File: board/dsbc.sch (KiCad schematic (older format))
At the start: 3 parts

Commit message: dev
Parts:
- removed U?: XC9572XL-VQ44, symbol custom:XC9572XL-VQ44
- added C?: 100n, symbol Device:C_Small
- added R?: R_Small, symbol Device:R_Small
- added U?: XC95144XL-TQ100, Package_QFP:TQFP-100_14x14mm_P0.5mm, symbol CPLD_Xilinx:XC95144XL-TQ100
- added U?: IS61C5128AL-10TLI, Package_SO:TSOP-II-44_10.16x18.41mm_P0.8mm, symbol Memory_RAM:IS61C5128AL-10TLI
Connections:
- net labels added: +3V3, A1, A10, A11, A12, A13, A14, A15, A16, A17, A18, A19, A2, A20, A21, A22, A23, A3, A4, A5, A6, A7, A8, A9, ADDR_INC, BE, BOOT, CLK_40MHz, CLK_CPU, D0, D1, D2, D3, D4, D5, D6, D7, E, GND, MLB, MX, RDY, R~W, TCK, TDI, TDO, TMS, VALID_ADDR, VDA, VPA, VPB, ~ABORT, ~IRQ, ~NMI, ~RESET_CPU
- wire segments 0 -> 9
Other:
- note added: "VALID_ADDR = VPA & VDA"

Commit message: dev
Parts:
- removed U?: P8X32A, symbol custom:P8X32A
- removed U?: XC95144XL-TQ100, Package_QFP:TQFP-100_14x14mm_P0.5mm, symbol CPLD_Xilinx:XC95144XL-TQ100
- added C?: 100n, symbol Device:C_Small
- added J?: Prop Plug, symbol Connector:Conn_01x04_Male
- added R?: R_Small, symbol Device:R_Small
- added U?: P8X32A-D40, Package_DIP:DIP-40_W15.24mm, symbol MCU_Parallax:P8X32A-D40
- added U?: XC9572XL-VQ64, Package_QFP:TQFP-64_10x10mm_P0.5mm, symbol CPLD_Xilinx:XC9572XL-VQ64
- added U?: 24LC512, symbol Memory_EEPROM:24LC512
- added U?: PS2_female, symbol custom:PS2_female
- added Y?: Crystal, symbol Device:Crystal
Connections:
- net labels added: B, DB0, DB1, DB2, DB3, DB4, DB5, DB6, DB7, G, HSYNC, MEM_ACC, MISO, MOSI, PROP_RST, PS2_CLK, PS2_DATA, R, RX, SCL, SCLK, SDA, TX, VSYNC, ~CS0, ~CS1, ~PROP_RST, ~RAM_CE, ~RAM_OE, ~RAM_WE
- net labels removed: ADDR_INC
- wire segments 9 -> 39
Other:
- note added: "MEM_ACC = VALID_ADDR & CLK_CPU"
- moved on the sheet: R?

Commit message: add 16mbit sram symbol
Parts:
- removed U?: XC9572XL-VQ64, Package_QFP:TQFP-64_10x10mm_P0.5mm, symbol CPLD_Xilinx:XC9572XL-VQ64
- removed U?: IS61C5128AL-10TLI, Package_SO:TSOP-II-44_10.16x18.41mm_P0.8mm, symbol Memory_RAM:IS61C5128AL-10TLI
- added U2: IS61WV20488FBLL-10TLI, Package_SO:TSOP-II-44_10.16x18.41mm_P0.8mm, symbol custom:IS61WV20488FBLL-10TLI
- added U3: XC95144XL-TQ100, Package_QFP:TQFP-100_14x14mm_P0.5mm, symbol CPLD_Xilinx:XC95144XL-TQ100
- gave numbers to parts that had none: 10
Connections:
- net labels added: B0, B1, CLK_50MHz, G0, G1, G2, R0, R1, R2, STOP_CPU, ~CS2
- net labels removed: B, CLK_40MHz, G, R

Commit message: added ps/2 connector
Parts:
- removed U4: PS2_female, symbol custom:PS2_female
- added C10, C11, C12, C3, C4, C5, C6, C7, C8, C9: 100n, Capacitor_SMD:C_0805_2012Metric_Pad1.15x1.40mm_HandSolder, symbol Device:C_Small
- added J2: Mini-DIN-6, custom:MINI-DIN-6-FULL-SHIELD, symbol Connector:Mini-DIN-6
- added R3, R4: R_Small, Resistor_SMD:R_0805_2012Metric_Pad1.15x1.40mm_HandSolder, symbol Device:R_Small
- added R5: 10k, Resistor_SMD:R_0805_2012Metric_Pad1.15x1.40mm_HandSolder, symbol Device:R_Small
- added R6, R7: 2k2, Resistor_SMD:R_0805_2012Metric_Pad1.15x1.40mm_HandSolder, symbol Device:R_Small
- C1, C2: footprint (none) -> Capacitor_SMD:C_0805_2012Metric_Pad1.15x1.40mm_HandSolder
- J1: footprint (none) -> Connector_PinHeader_2.54mm:PinHeader_1x04_P2.54mm_Vertical
- R1, R2: footprint (none) -> Resistor_SMD:R_0805_2012Metric_Pad1.15x1.40mm_HandSolder
- U1: footprint (none) -> Package_DIP:DIP-40_W15.24mm
- U6: footprint (none) -> Package_DIP:DIP-8_W7.62mm_Socket
- Y1: footprint (none) -> Crystal:Resonator-2Pin_W10.0mm_H5.0mm
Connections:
- net labels removed: PROP_RST
- wire segments 39 -> 105
- no-connect marks 0 -> 2
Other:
- moved on the sheet: U3, U6

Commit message: spartan branch
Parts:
- removed C10, C11, C12, C2, C3, C4, C5, C6, C7, C8, C9: 100n, Capacitor_SMD:C_0805_2012Metric_Pad1.15x1.40mm_HandSolder, symbol Device:C_Small
- removed J1: Prop Plug, Connector_PinHeader_2.54mm:PinHeader_1x04_P2.54mm_Vertical, symbol Connector:Conn_01x04_Male
- removed J2: Mini-DIN-6, custom:MINI-DIN-6-FULL-SHIELD, symbol Connector:Mini-DIN-6
- removed R1, R2, R3, R4: R_Small, Resistor_SMD:R_0805_2012Metric_Pad1.15x1.40mm_HandSolder, symbol Device:R_Small
- removed R5: 10k, Resistor_SMD:R_0805_2012Metric_Pad1.15x1.40mm_HandSolder, symbol Device:R_Small
- removed R6, R7: 2k2, Resistor_SMD:R_0805_2012Metric_Pad1.15x1.40mm_HandSolder, symbol Device:R_Small
- removed U2: IS61WV20488FBLL-10TLI, Package_SO:TSOP-II-44_10.16x18.41mm_P0.8mm, symbol custom:IS61WV20488FBLL-10TLI
- removed U3: XC95144XL-TQ100, Package_QFP:TQFP-100_14x14mm_P0.5mm, symbol CPLD_Xilinx:XC95144XL-TQ100
- removed U5: P8X32A-D40, Package_DIP:DIP-40_W15.24mm, symbol MCU_Parallax:P8X32A-D40
- removed U6: 24LC512, Package_DIP:DIP-8_W7.62mm_Socket, symbol Memory_EEPROM:24LC512
- removed Y1: Crystal, Crystal:Resonator-2Pin_W10.0mm_H5.0mm, symbol Device:Crystal
- added J? (x2): Conn_02x20_Odd_Even, symbol Connector_Generic:Conn_02x20_Odd_Even
- added J?: DB15_Female_HighDensity, symbol Connector:DB15_Female_HighDensity
- added R? (x8): R_Small, symbol Device:R_Small
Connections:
- net labels added: +5V, B, G
- net labels removed: A16, A17, A18, A19, A20, A21, A22, A23, BOOT, CLK_50MHz, D0, D1, D2, D3, D4, D5, D6, D7, E, MEM_ACC, MISO, MOSI, MX, PS2_CLK, PS2_DATA, RX, SCL, SCLK, SDA, STOP_CPU, TCK, TDI, TDO, TMS, TX, VALID_ADDR, ~CS0, ~CS1, ~CS2, ~PROP_RST, ~RAM_CE, ~RAM_OE, ~RAM_WE
- wire segments 105 -> 32
- no-connect marks 2 -> 22
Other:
- note added: "0,7V max.\nRGB-Kanal: Widerstände zusammen 270 Ohm.\nIm Monitor sind 75 Ohm gegen GND."
- note added: "A16"
- note added: "A17"
- note added: "CCLK"
- note added: "DONE"
- note added: "FPGA-DOUT"
- note added: "INIT_B"
- note added: "JTAG-ISO"
- note added: "PROG_B"
- note added: "TCK"
- note added: "TDO"
- note added: "TMS"
- note added: "~SRAM_OE"
- note added: "~SRAM_WE"
- note removed: "MEM_ACC = VALID_ADDR & CLK_CPU"
- note removed: "VALID_ADDR = VPA & VDA"

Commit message: schematic: add resistor to RDY pin
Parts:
- added R?: R_Small, symbol Device:R_Small
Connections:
- wire segments 32 -> 34
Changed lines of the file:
@@
 Text Label 2500 2150 0    50   ~ 0
 ~ABORT
-Text Label 2500 2050 0    50   ~ 0
+Text Label 3000 2050 0    50   ~ 0
 RDY
 Text Label 2500 1950 0    50   ~ 0
@@
 Text Notes 1300 5750 0    50   ~ 0
 0,7V max.\nRGB-Kanal: Widerstände zusammen 270 Ohm.\nIm Monitor sind 75 Ohm gegen GND.
+Wire Wire Line
+	2500 2050 2750 2050
+$Comp
+L Device:R_Small R?
+U 1 1 5D2CC268
+P 2850 2050
+F 0 "R?" V 2654 2050 50  0000 C CNN
+F 1 "R_Small" V 2745 2050 50  0000 C CNN
+F 2 "" H 2850 2050 50  0001 C CNN
+F 3 "~" H 2850 2050 50  0001 C CNN
+	1    2850 2050
+	0    1    1    0
+$EndComp
+Wire Wire Line
+	2950 2050 3000 2050
 $EndSCHEMATC

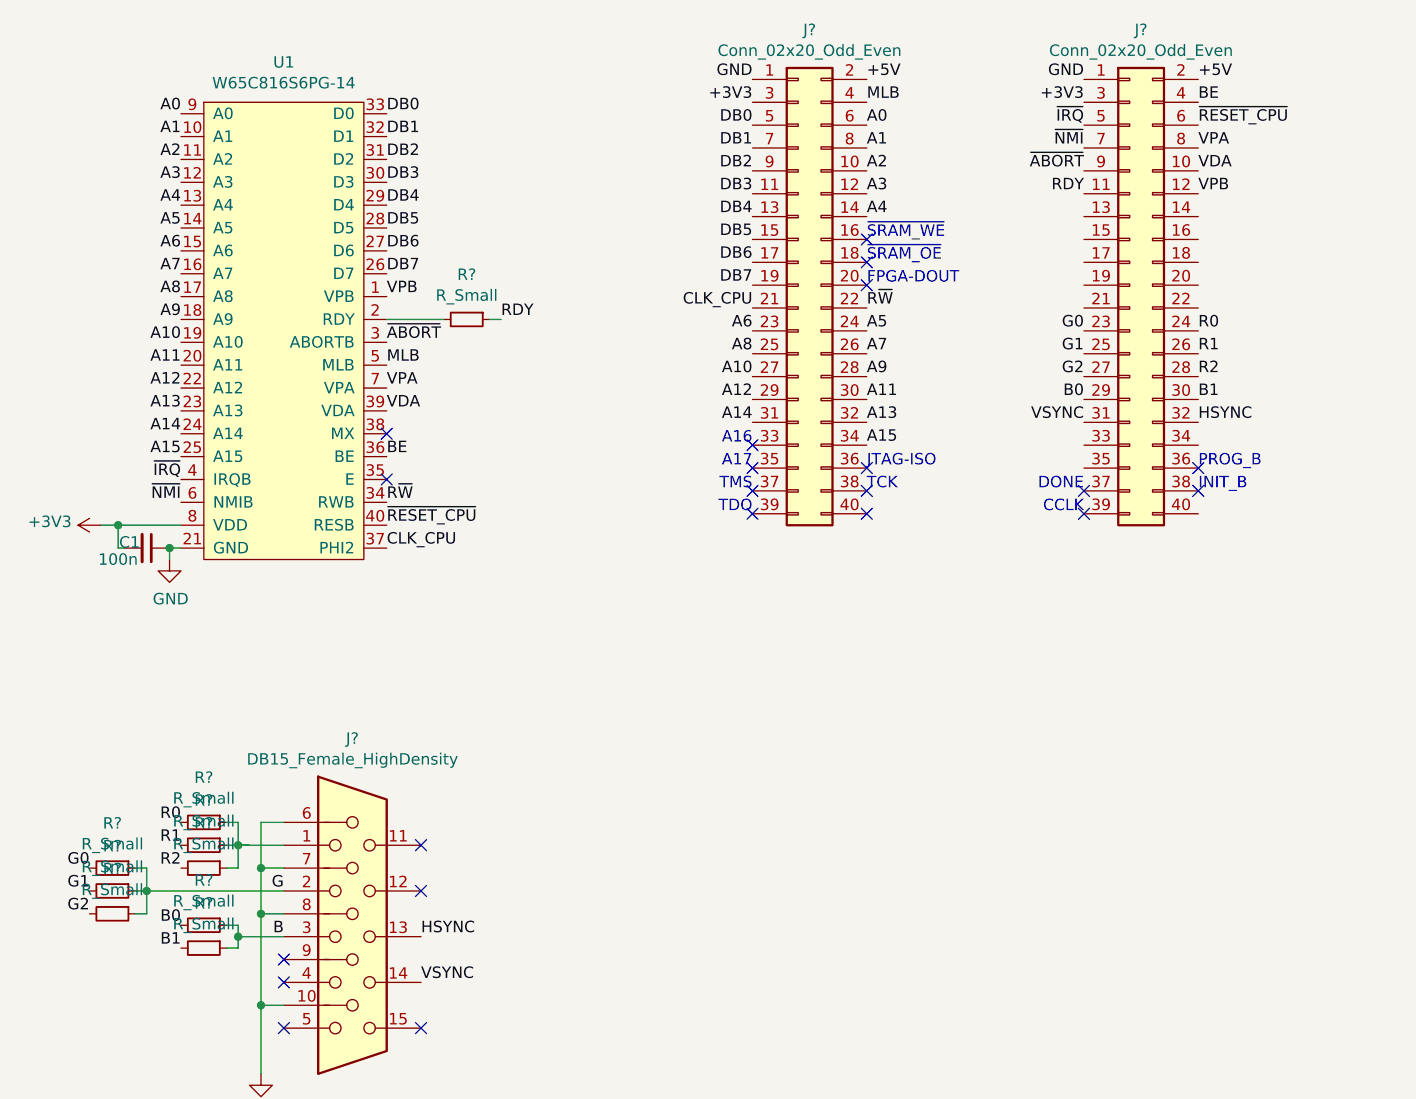
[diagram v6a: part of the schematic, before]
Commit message: schematic: eeprom, resistors board: placement
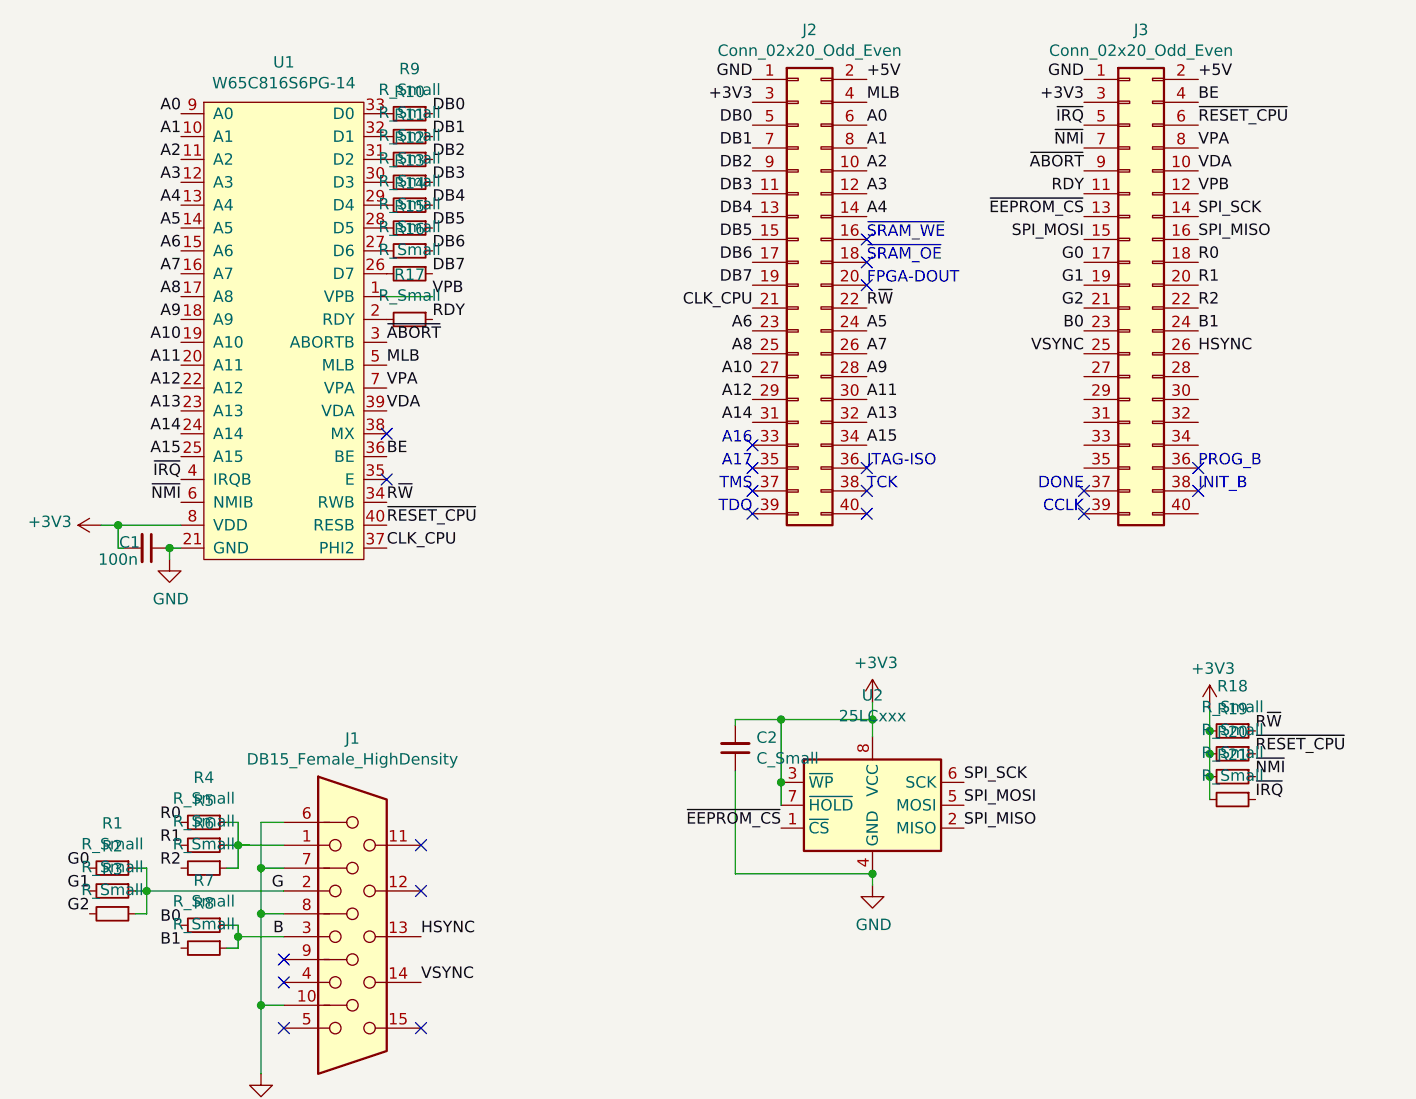
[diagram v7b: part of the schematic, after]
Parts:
- added C2: C_Small, Capacitor_SMD:C_0805_2012Metric_Pad1.15x1.40mm_HandSolder, symbol Device:C_Small
- added R10, R11, R12, R13, R14, R15, R16, R18, R19, R20, R21, R9: R_Small, Resistor_SMD:R_0805_2012Metric_Pad1.15x1.40mm_HandSolder, symbol Device:R_Small
- added U2: 25LCxxx, Package_DIP:DIP-8_W7.62mm_LongPads, symbol Memory_EEPROM:25LCxxx
- J1: renamed from J?; footprint (none) -> Connector_Dsub:DSUB-15-HD_Female_Horizontal_P2.29x1.98mm_EdgePinOffset9.40mm
- J2, J3: renamed from J?; footprint (none) -> Connector_PinHeader_2.54mm:PinHeader_2x20_P2.54mm_Horizontal
- R1, R17, R2, R3, R4, R5, R6, R7, R8: renamed from R?; footprint (none) -> Resistor_SMD:R_0805_2012Metric_Pad1.15x1.40mm_HandSolder
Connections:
- net labels added: SPI_MISO, SPI_MOSI, SPI_SCK, ~EEPROM_CS
- wire segments 34 -> 47
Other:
- moved on the sheet: R17

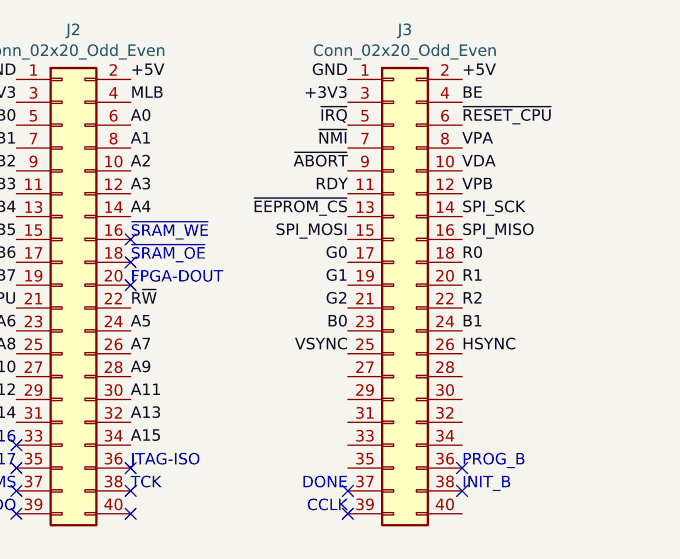
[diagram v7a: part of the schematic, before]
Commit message: board: placement. pin headers have wrong orientation
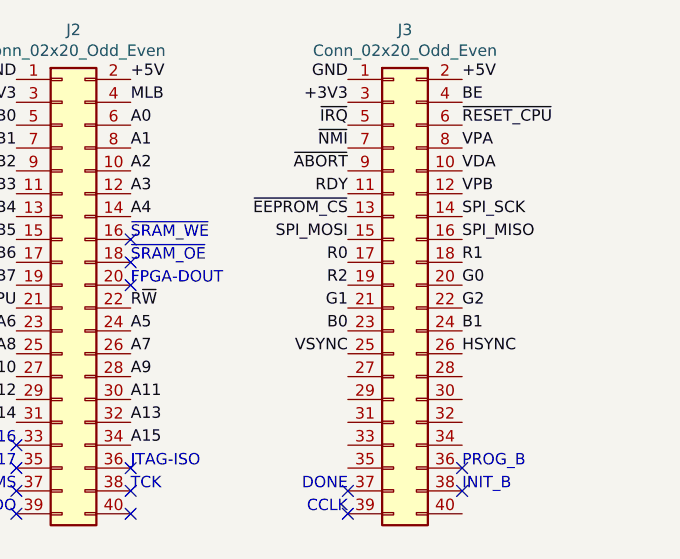
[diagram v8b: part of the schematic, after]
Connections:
- net G0: now also J3.20 (Pin_20); no longer J3.17 (Pin_17)
- net G1: now also J3.21 (Pin_21); no longer J3.19 (Pin_19)
- net G2: now also J3.22 (Pin_22); no longer J3.21 (Pin_21)
- net R0: now also J3.17 (Pin_17); no longer J3.18 (Pin_18)
- net R1: now also J3.18 (Pin_18); no longer J3.20 (Pin_20)
- net R2: now also J3.19 (Pin_19); no longer J3.22 (Pin_22)
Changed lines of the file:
@@
 NoConn ~ 2050 4850
 NoConn ~ 2650 4550
+Text Label 5550 1800 2    50   ~ 0
+R0
 Text Label 6050 1800 0    50   ~ 0
-R0
+R1
+Text Label 5550 1900 2    50   ~ 0
+R2
 Text Label 6050 1900 0    50   ~ 0
-R1
+G0
+Text Label 5550 2000 2    50   ~ 0
+G1
 Text Label 6050 2000 0    50   ~ 0
-R2
-Text Label 5550 1800 2    50   ~ 0
-G0
-Text Label 5550 1900 2    50   ~ 0
-G1
-Text Label 5550 2000 2    50   ~ 0
 G2
 Text Label 5550 2100 2    50   ~ 0
